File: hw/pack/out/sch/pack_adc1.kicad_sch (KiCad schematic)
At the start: 15 parts, among them U2 PCM1840

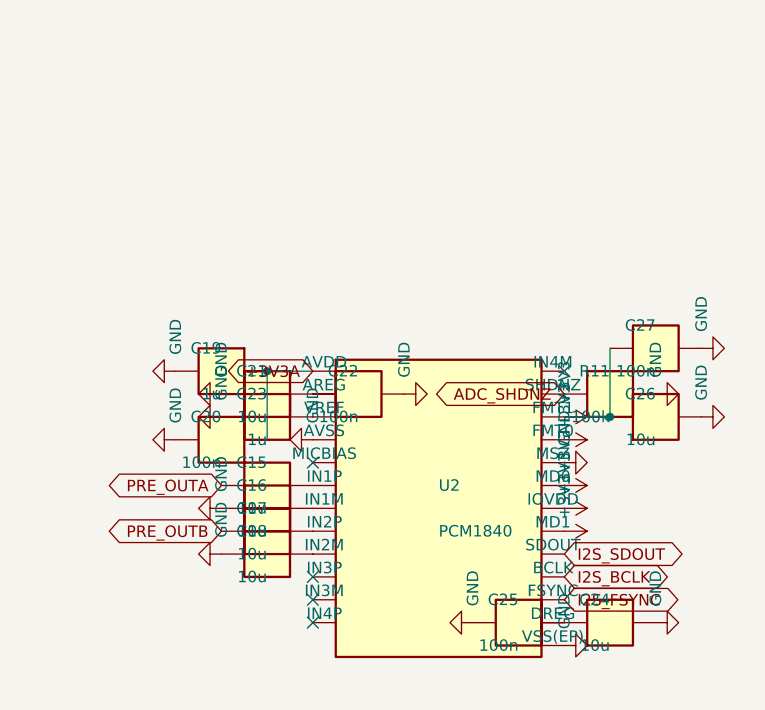
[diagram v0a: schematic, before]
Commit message: hw/pack: review fixes for #75 (op-amp CM, hot-plug protection, CI, cutoff, LEDs) (#31)
- VCM 180k/100k (1.77 V) keeps OPA1656 +IN inside V+ - 2.25 V; SPICE clamp 0.25/4.70 V,
  test asserts input CM, ADC pin (1.375 V) and prints numbers in CI (-rP)
- tip ESD (TPD1E10B06), BAV199 clamp + 100R ahead of the op-amp; C9 22p; noise 0.96 uV
- CI installs skidl==3.0.0, pack test fails (not skips) under CI, stale-output diff check
- no PTC; cell sensed at BAT+; firmware cutoff 3.2 V derived in audit.py; PK-8 LED
  thresholds -10/-7 dBFS; real LED MPNs; VDDH decoupling; audit prints DK-price BOM

Co-Authored-By: Claude Opus 5.5 <noreply@anthropic.com>
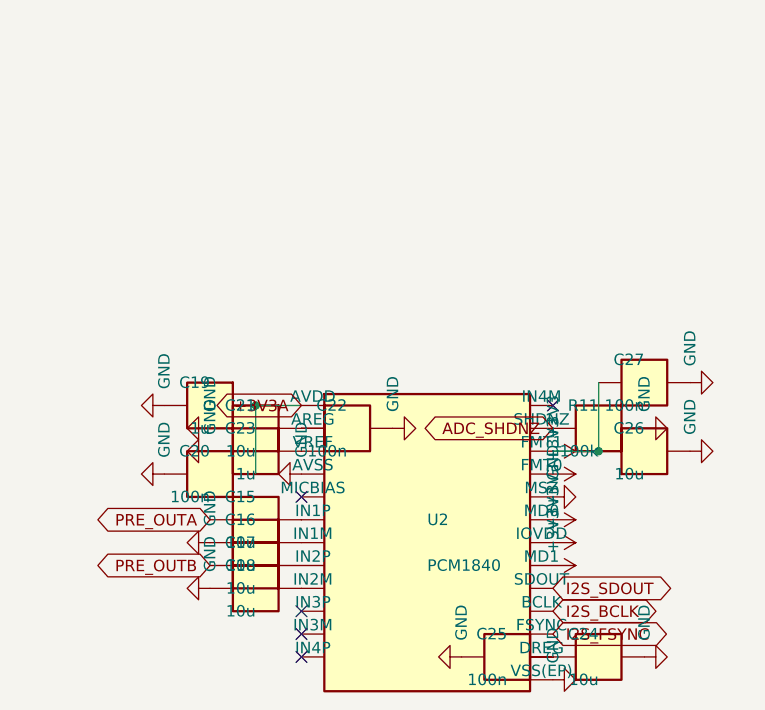
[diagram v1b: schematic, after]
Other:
- moved on the sheet: C15, C16, C17, C18, C19, C20, C21, C22, C23, C24, C25, C26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

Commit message: hw/pack: 3 A chip fuse (23 mOhm) on BAT+, cutoff re-derived, BOM $34.98 (#31)
Co-Authored-By: Claude Opus 5.5 <noreply@anthropic.com>
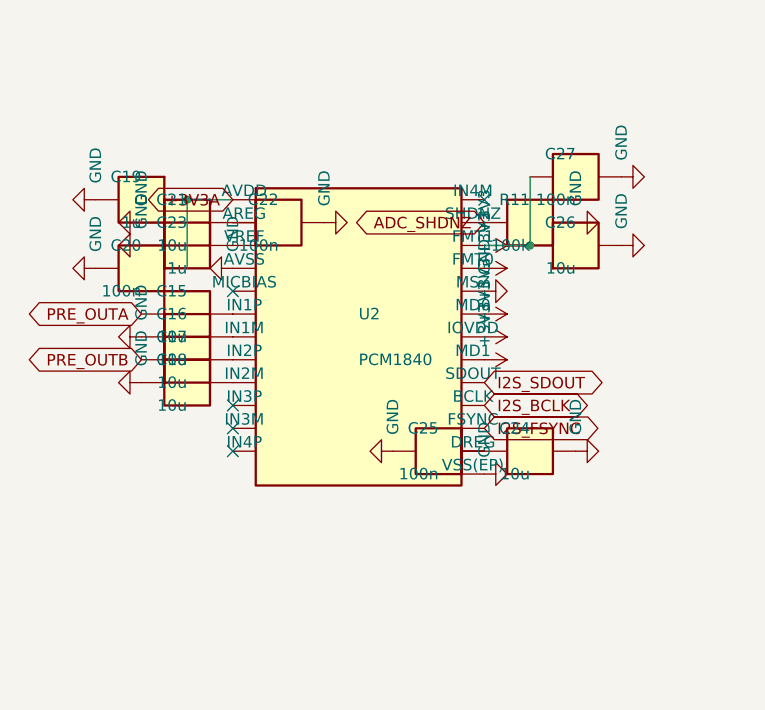
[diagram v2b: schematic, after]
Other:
- moved on the sheet: C15, C16, C17, C18, C19, C20, C21, C22, C23, C24, C25, C26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

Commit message: pack: restore battery-sense divider (R13/C30) (#84)
* hw/pack: restore battery-sense divider R13/C30 hidden in a comment

Co-Authored-By: Claude Sonnet 5.5 <noreply@anthropic.com>

* tests: cite nRF5340 SAADC pin limit (VDD) from the product spec

Co-Authored-By: Claude Sonnet 5.5 <noreply@anthropic.com>

* hw/pack: price 0402 resistors and 100n caps from LCSC qty-100 pages; UK BOM refs; merge main

Co-Authored-By: Claude Sonnet 5.5 <noreply@anthropic.com>

---------

Co-authored-by: Claude Sonnet 5.5 <noreply@anthropic.com>
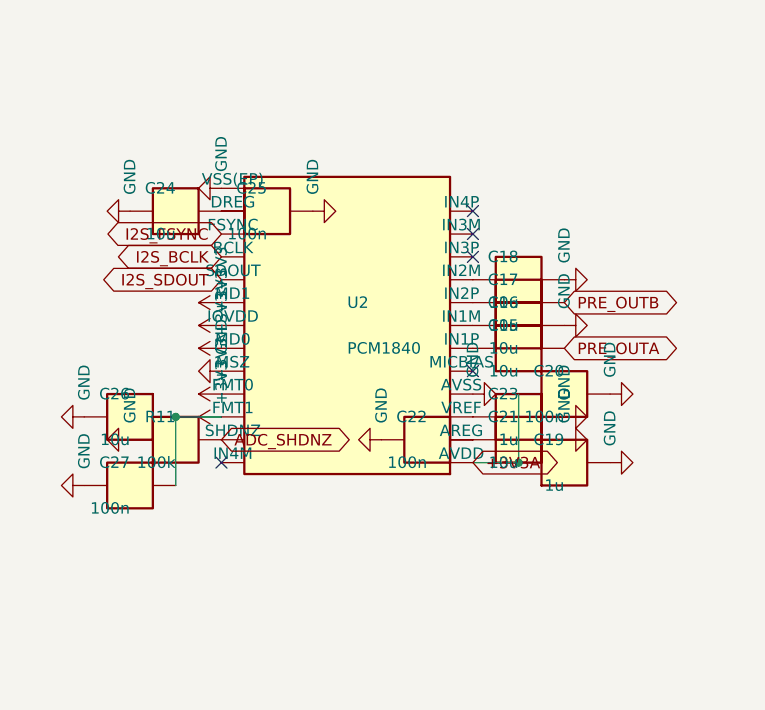
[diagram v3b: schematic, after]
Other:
- moved on the sheet: C15, C16, C17, C18, C19, C20, C21, C22, C23, C24, C25, C26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

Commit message: pack: cost-down to PK-12 $33.34: printed cell cradle + MYOUNG contacts, LCSC IPEX pigtail, priced M2 screws (#34)
- BT1: MYOUNG MY-18650-04-J/-05-J (LCSC C19184125/C19184124) in a printed
  cradle in the base (76 mm plate faces: spring 4.2-9.2 mm for 70-65 mm cells);
  the SMT BH-18650-B1BA002 holder is gone; footprint Cell_Wire_Pads
- pigtail: BAT Wireless BWIPX1-SMA-1.13L150 (LCSC C784404, $0.6015 @100), SMA
  cut off, ~100 mm + 31 mm wire whip; audit.py PIGTAIL_IL 0.46 <= 0.6 dB
- audit.py cutoff path includes the spring (0.10 ohm), cutoff stays 3.2 V
- 2 x M2x6 PT screws $0.112 (Fastener Superstore 585907)
- prices.py, bom.csv, pack_uk.csv (UK $34.81) updated

Co-Authored-By: Claude Opus 5.5 <noreply@anthropic.com>
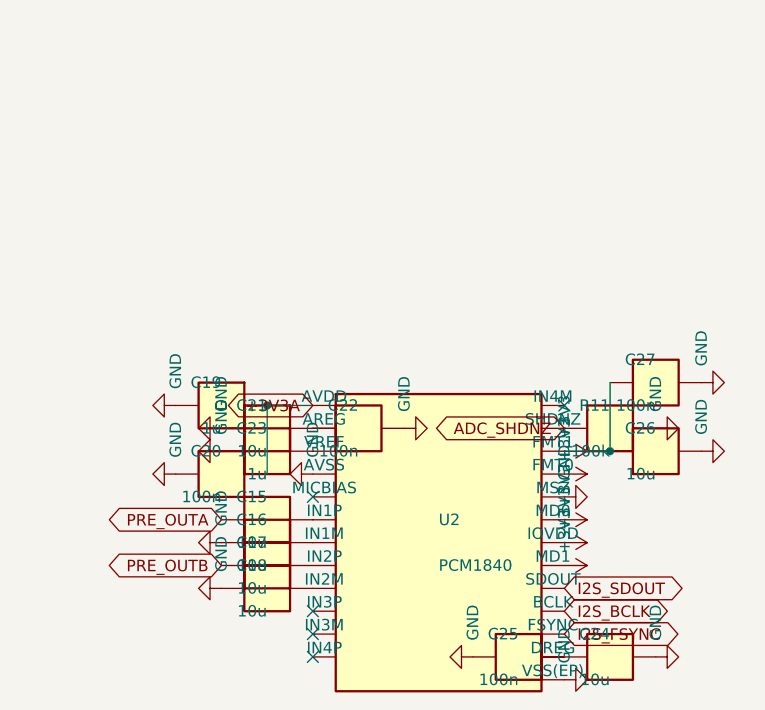
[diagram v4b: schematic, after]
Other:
- moved on the sheet: C15, C16, C17, C18, C19, C20, C21, C22, C23, C24, C25, C26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

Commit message: pack: #104 review fixes: 1 mm L1 battery path, test points, clip inserts off the antenna, pigtail route, JLC LCSC/rotations (#34)
- router: 'bat' class (1.0 mm, L1 only, necks <=1.36 mm at small pads);
  SW1 on-throw moved to pin 3 so feed and VSYS don't cross; 40 mOhm path
- audit.py: cell path from the board tracks (121 mOhm total, est. spring):
  cutoff computes 3.2012 V -> rounds to 3.3 V (reported, not tuned)
- TP3-TP11 folded in from review-104-tps (415194b), TP5/TP9-11 moved
- mech: clip inserts to (-24,3)/(-24,17) under the board; PIGTAIL route,
  bend radius, tie-down; fit.py checks both
- outputs: LCSC # per BOM line (verified), DNP/CONSIGN, CPL rotation table
- tests: battery path layer/width/R, BOM LCSC-or-DNP, rotation table

Co-Authored-By: Claude Opus 5.5 <noreply@anthropic.com>
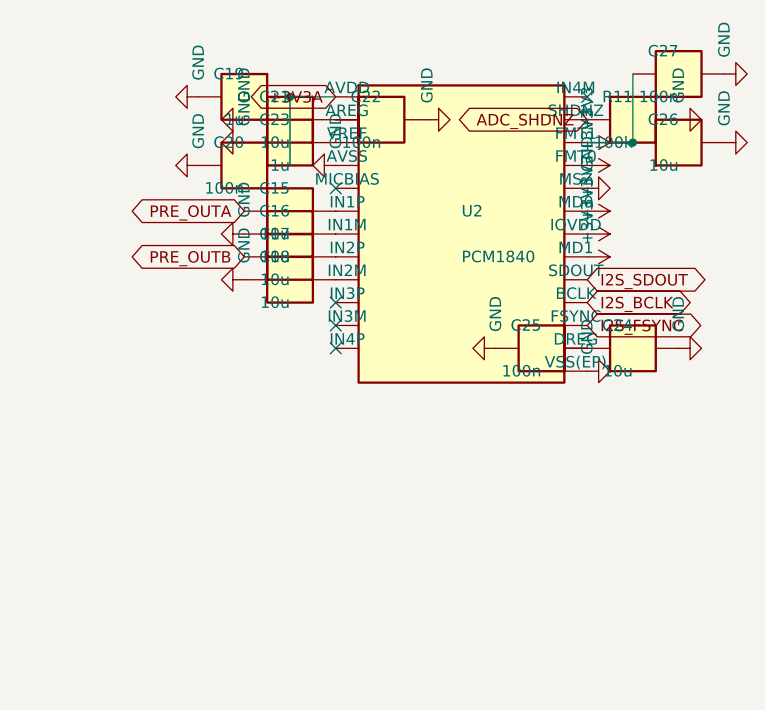
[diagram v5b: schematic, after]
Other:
- moved on the sheet: C15, C16, C17, C18, C19, C20, C21, C22, C23, C24, C25, C26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
